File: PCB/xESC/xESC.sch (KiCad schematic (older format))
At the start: 16 parts, among them U1 ATmega328-AU, Y1 Resonator

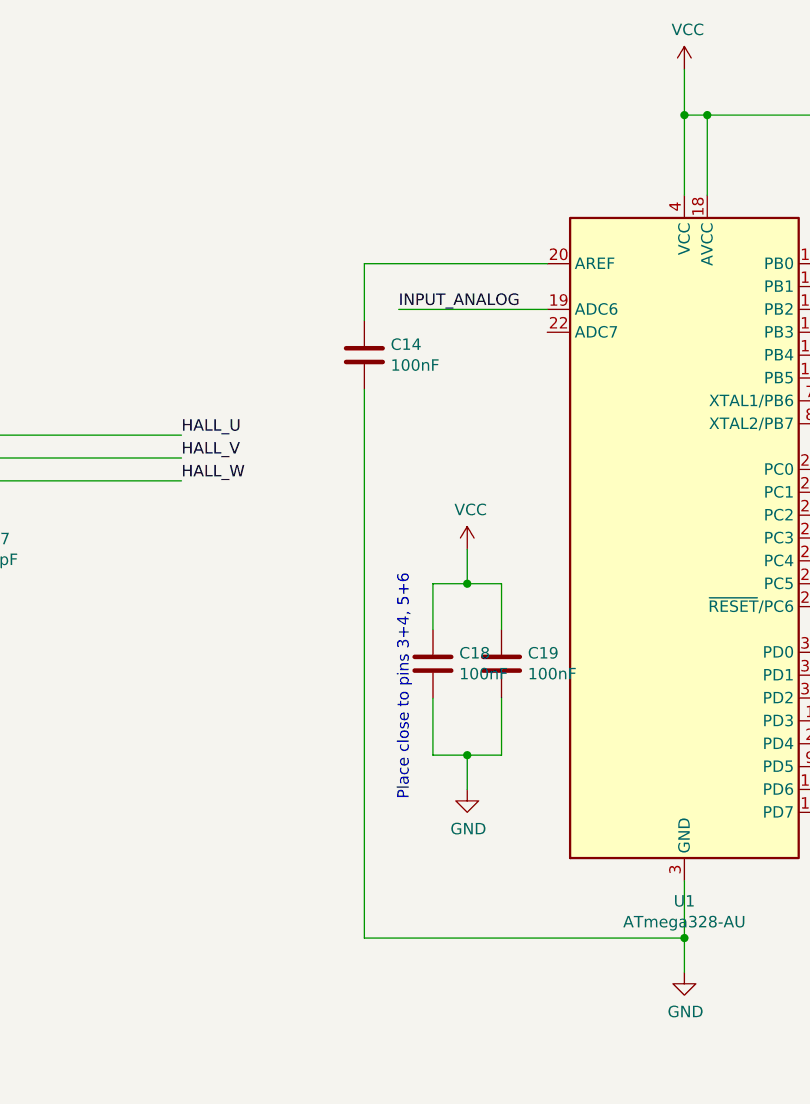
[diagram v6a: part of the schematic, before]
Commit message: added VM to analog input, added zener diode for over voltage protection, added LED to drv_enable, shunt now 3mOhms, added jumper for TMC6100's test pin
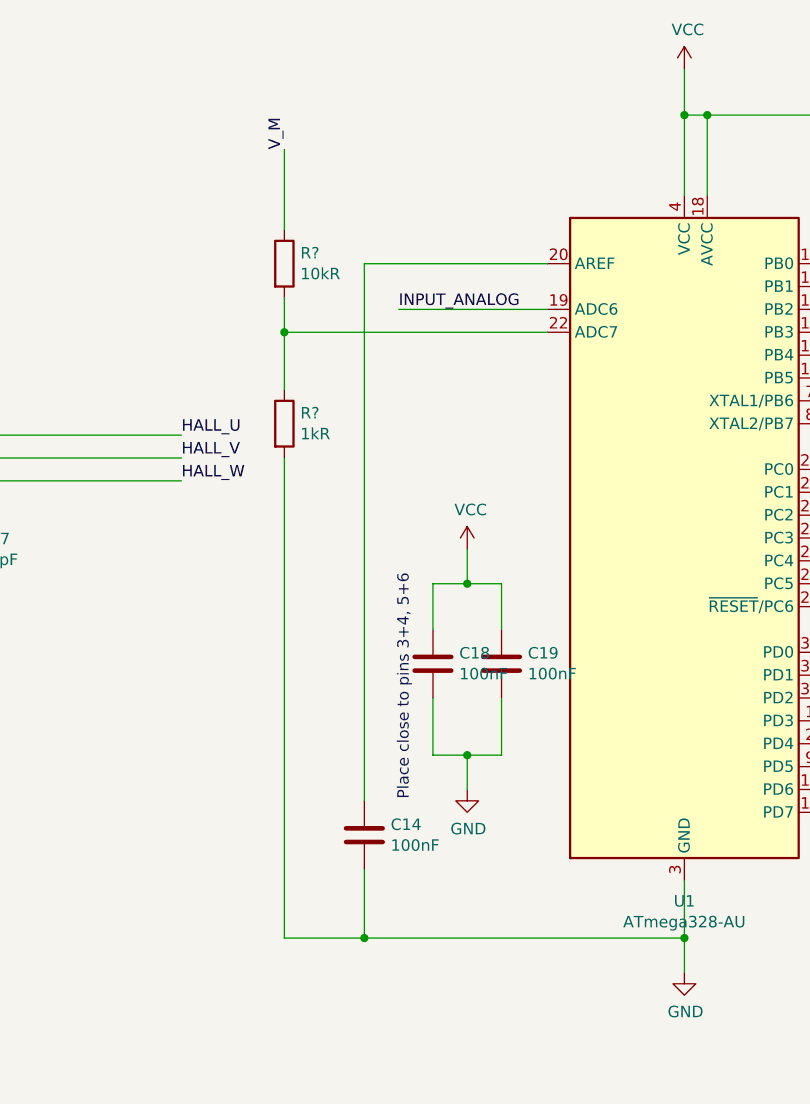
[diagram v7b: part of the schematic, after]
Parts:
- added R?: 10kR, Resistor_SMD:R_0805_2012Metric, symbol Device:R
- added R?: 1kR, Resistor_SMD:R_0805_2012Metric, symbol Device:R
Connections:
- net GND: now also R?.2
- net V_M: now also R?.1
- net at U1.22 (ADC7): now also R?.1, R?.2
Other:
- moved on the sheet: C14
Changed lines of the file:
@@
 L Device:C C?
 U 1 1 6181D81C
-P 4700 2800
+P 4700 4900
 AR Path="/6183112C/6181D81C" Ref="C?"  Part="1"
 AR Path="/6181D81C" Ref="C14"  Part="1"
-F 0 "C14" H 4815 2846 50  0000 L CNN
-F 1 "100nF" H 4815 2755 50  0000 L CNN
-F 2 "Capacitor_SMD:C_0805_2012Metric_Pad1.18x1.45mm_HandSolder" H 4738 2650 50  0001 C CNN
-F 3 "~" H 4700 2800 50  0001 C CNN
-	1    4700 2800
-	1    0    0    -1
-$EndComp
-Wire Wire Line
-	4700 2400 4700 2650
+F 0 "C14" H 4815 4946 50  0000 L CNN
+F 1 "100nF" H 4815 4855 50  0000 L CNN
+F 2 "Capacitor_SMD:C_0805_2012Metric_Pad1.18x1.45mm_HandSolder" H 4738 4750 50  0001 C CNN
+F 3 "~" H 4700 4900 50  0001 C CNN
+	1    4700 4900
+	1    0    0    -1
+$EndComp
+Wire Wire Line
+	4700 2400 4700 4750
 Wire Wire Line
 	4700 2400 5500 2400
 Wire Wire Line
-	4700 2950 4700 5350
+	4700 5050 4700 5350
 Wire Wire Line
 	4700 5350 6100 5350
@@
 Text Label 1850 4650 0    50   ~ 0
 EXT_SPI_SS
+Wire Wire Line
+	4350 2700 5500 2700
+Text Label 4350 1900 1    50   ~ 0
+V_M
+$Comp
+L Device:R R?
+U 1 1 6186A5D0
+P 4350 2400
+F 0 "R?" H 4420 2446 50  0000 L CNN
+F 1 "10kR" H 4420 2355 50  0000 L CNN
+F 2 "Resistor_SMD:R_0805_2012Metric" V 4280 2400 50  0001 C CNN
+F 3 "~" H 4350 2400 50  0001 C CNN
+	1    4350 2400
+	1    0    0    -1
+$EndComp
+$Comp
+L Device:R R?
+U 1 1 6186EEE1
+P 4350 3100
+F 0 "R?" H 4420 3146 50  0000 L CNN
+F 1 "1kR" H 4420 3055 50  0000 L CNN
+F 2 "Resistor_SMD:R_0805_2012Metric" V 4280 3100 50  0001 C CNN
+F 3 "~" H 4350 3100 50  0001 C CNN
+	1    4350 3100
+	1    0    0    -1
+$EndComp
+Wire Wire Line
+	4350 1900 4350 2250
+Wire Wire Line
+	4350 2550 4350 2700
+Wire Wire Line
+	4350 2700 4350 2950
+Connection ~ 4350 2700
+Wire Wire Line
+	4350 3250 4350 5350
+Wire Wire Line
+	4350 5350 4700 5350
+Connection ~ 4700 5350
 $EndSCHEMATC

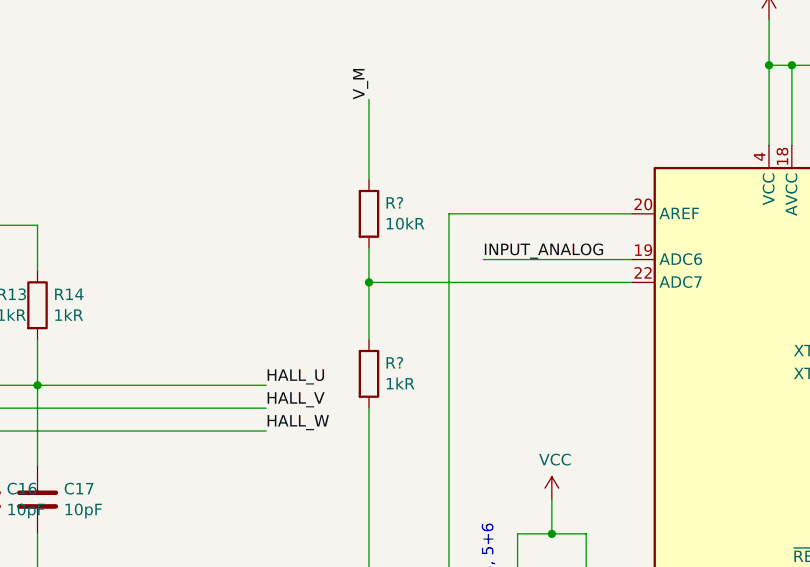
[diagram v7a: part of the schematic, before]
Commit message: fixed silkscreen
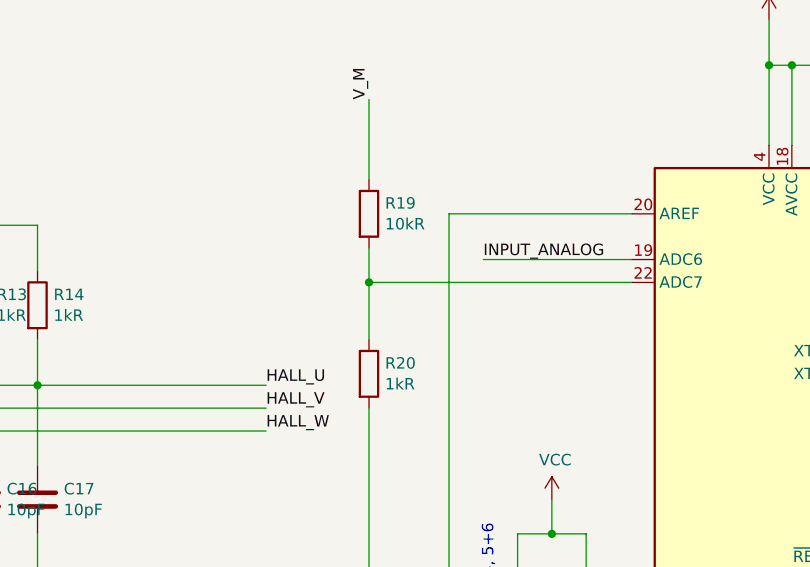
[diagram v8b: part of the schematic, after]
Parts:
- gave numbers to parts that had none: 2
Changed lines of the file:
@@
 V_M
 $Comp
-L Device:R R?
+L Device:R R19
 U 1 1 6186A5D0
 P 4350 2400
-F 0 "R?" H 4420 2446 50  0000 L CNN
+F 0 "R19" H 4420 2446 50  0000 L CNN
 F 1 "10kR" H 4420 2355 50  0000 L CNN
 F 2 "Resistor_SMD:R_0805_2012Metric" V 4280 2400 50  0001 C CNN
@@
 $EndComp
 $Comp
-L Device:R R?
+L Device:R R20
 U 1 1 6186EEE1
 P 4350 3100
-F 0 "R?" H 4420 3146 50  0000 L CNN
+F 0 "R20" H 4420 3146 50  0000 L CNN
 F 1 "1kR" H 4420 3055 50  0000 L CNN
 F 2 "Resistor_SMD:R_0805_2012Metric" V 4280 3100 50  0001 C CNN
